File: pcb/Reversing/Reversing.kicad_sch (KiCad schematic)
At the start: 20 parts, among them Q1 S9015, U1 CH340G, U2 MAX485E, Y1 12Mhz

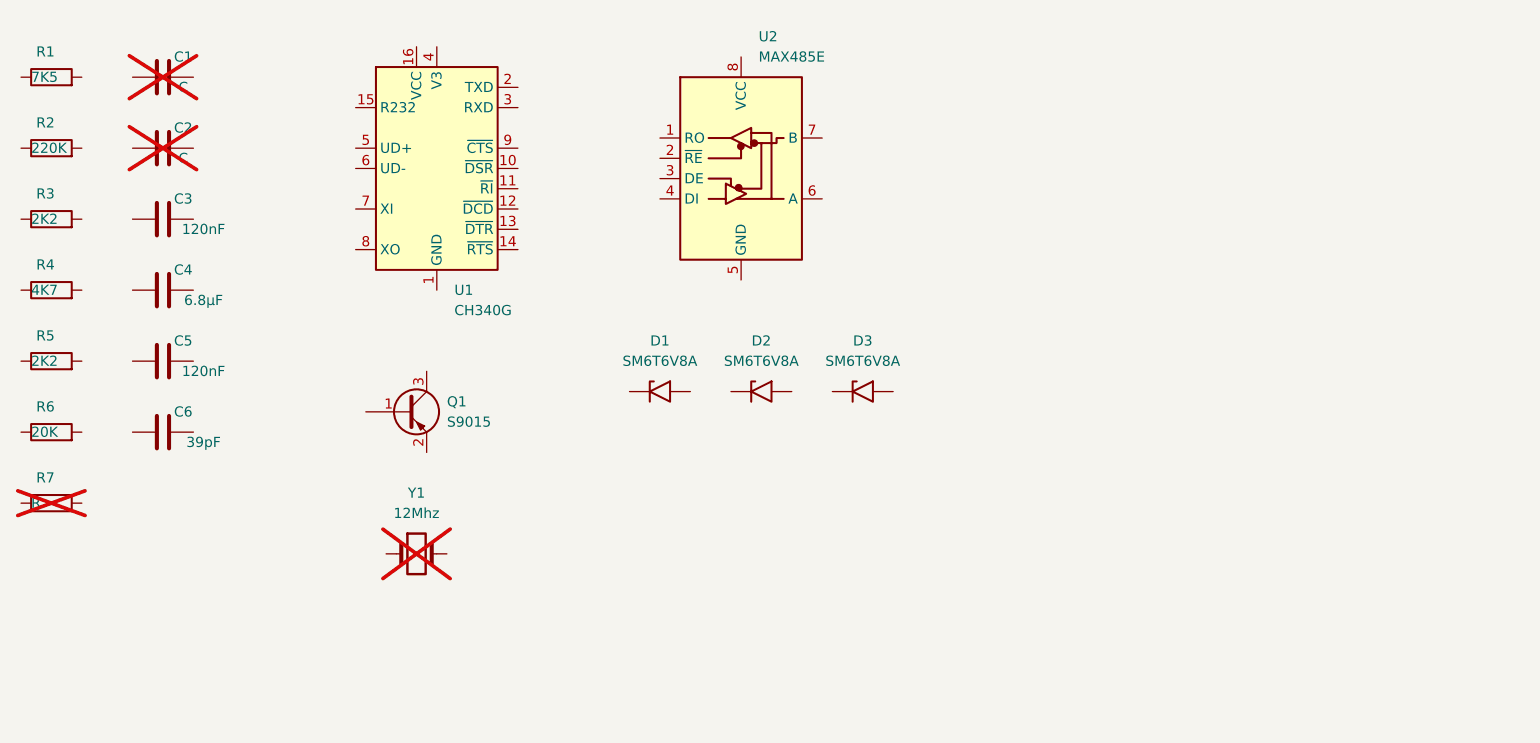
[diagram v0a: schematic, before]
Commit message: Reverse whole board in one swoop
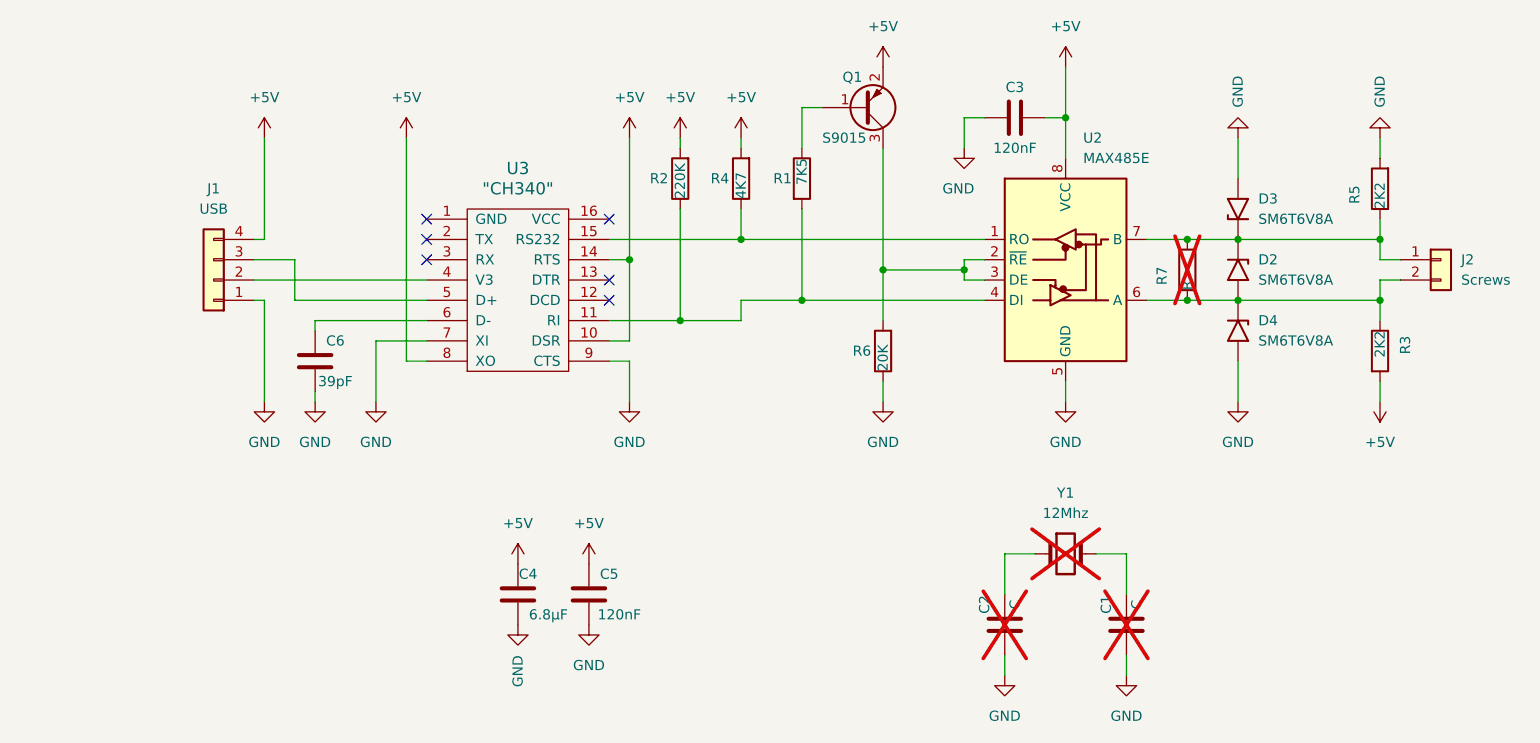
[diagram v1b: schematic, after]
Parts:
- removed U1: CH340G, Package_SO:SOIC-16_3.9x9.9mm_P1.27mm, symbol Interface_USB:CH340G
- added J1: USB, Connector_PinHeader_2.54mm:PinHeader_1x04_P2.54mm_Vertical, symbol Connector_Generic:Conn_01x04
- added J2: Screws, Connector_PinHeader_2.54mm:PinHeader_1x02_P2.54mm_Vertical, symbol Connector_Generic:Conn_01x02
- added U3: "CH340", Package_SO:SOIC-16_3.9x9.9mm_P1.27mm, symbol MeineBib:CH340G
- C1, C2, C3, C5, C6: footprint (none) -> Capacitor_SMD:C_0603_1608Metric
- C4: footprint (none) -> Capacitor_SMD:C_0805_2012Metric
- D2, D3: footprint Diode_SMD:D_SMB -> Diode_SMD:D_SOD-123
- D4: renamed from D1; footprint Diode_SMD:D_SMB -> Diode_SMD:D_SOD-123
- R1, R2, R3, R4, R5, R6, R7: footprint (none) -> Resistor_SMD:R_0603_1608Metric
- U2: footprint (none) -> Package_SO:SO-8_3.9x4.9mm_P1.27mm
- Y1: footprint (none) -> Crystal:Crystal_HC18-U_Vertical
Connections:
- net GND: now reaches C1.1
- net GND: now also C2.1, C3.2, C4.2, C5.1, C6.2, D3.2 (A2), D4.2 (A2), R5.2, R6.1, U2.5 (GND), J1.1 (Pin_1), U3.7 (XI), U3.9 (CTS)
- net at C1.2: now also Y1.2
- net at C2.2: now also Y1.1
- net at D2.1 (A1): now also D3.1 (A1), R5.1, R7.2, U2.7 (B), J2.1 (Pin_1)
- net at D2.2 (A2): now also D4.1 (A1), R3.1, R7.1, U2.6 (A), J2.2 (Pin_2)
- net at R2.1: now also R1.2, U2.4 (DI), U3.11 (RI)
- net +5V: now reaches R2.2
- net +5V: now also C3.1, C4.1, C5.2, Q1.2 (E), R3.2, R4.2, U2.8 (VCC), J1.4 (Pin_4), U3.10 (DSR), U3.14 (RTS), U3.8 (XO)
- net at Q1.1 (B): now also R1.1
- net at Q1.3 (C): now also R6.2, U2.2 (~{RE}), U2.3 (DE)
- net at R4.1: now also U2.1 (RO), U3.15 (RS232)
- net at C6.1: now also U3.6 (D-)
- new net: J1.2 (Pin_2), U3.4 (V3)
- new net: J1.3 (Pin_3), U3.5 (D+)
- no-connect marks 0 -> 6
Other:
- moved on the sheet: C1, C2, C3, C4, C5, C6, D2, D3, D4, Q1, R1, R2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
